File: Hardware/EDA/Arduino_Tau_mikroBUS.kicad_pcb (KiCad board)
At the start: 4 copper layers, 38.1 x 69.8 mm, 30 parts, among them J1 HEADER_F_2.54MM_1R8P_ST_AU_PTH, J2 HEADER_F_2.54MM_1R8P_ST_AU_PTH, J3 HEADER_F_2.54MM_1R11P_ST_AU_P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, J4 HEADER_F_2.54MM_1R11P_ST_AU_P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, J5 Molex_0475710001, M1 FID, M2 FID, M3 FID, P1 HEADER_M_2.54MM_1R4P_ST_AU_PTH, P2 HEADER_M_2.54MM_1R4P_ST_AU_PTH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

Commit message: Updated schematic and gerbers. Added silkscreen artwork and 3D component models.
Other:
- board text added: "Arduino Tau mikroBUS Dev Board"
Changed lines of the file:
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@@
     (area 60.884999 31.674999 99.135001 101.675001)
     (thickness 1.6)
-    (drawings 26)
+    (drawings 27)
     (tracks 249)
     (zones 0)
@@
     (pad 1 thru_hole rect (at -12.7 0 270) (size 1.397 1.397) (drill 0.79375) (layers *.Cu *.Mask F.SilkS)
       (net 5 D5))
+    (model C:/Engineering/KiCAD_Libraries/3D/Headers/VRML/Harwin_M20-7821146.wrl
+      (at (xyz 0 0 0))
+      (scale (xyz 1 1 1))
+      (rotate (xyz 0 0 0))
+    )
   )
   (module Active:SO-8 (layer F.Cu)
@@
     (pad 1 thru_hole rect (at -12.7 0 270) (size 1.397 1.397) (drill 0.79375) (layers *.Cu *.Mask F.SilkS)
       (net 18 D8))
+    (model C:/Engineering/KiCAD_Libraries/3D/Headers/VRML/HEADER_F_2.54MM_1R11P_ST_AU_PTH.wrl
+      (at (xyz 0 0 0))
+      (scale (xyz 1 1 1))
+      (rotate (xyz 0 0 0))
+    )
   )
   (module Passive:0603 (layer F.Cu)
@@
     (pad 4 thru_hole circle (at 3.81 0) (size 1.7272 1.7272) (drill 0.9906) (layers *.Cu *.Mask)
       (net 9 5.0V))
+    (model C:/Engineering/KiCAD_Libraries/3D/Power_Supplies/DC_DC_Converters/VRML/RECOM_RM-0505S.wrl
+      (at (xyz 0 0 0))
+      (scale (xyz 1 1 1))
+      (rotate (xyz 0 0 0))
+    )
+  )
+  (gr_text "Arduino Tau\nmikroBUS\nDev Board" (at 91.186 86.868 90) (layer F.SilkS)
+    (effects (font (size 1.27 1.27) (thickness 0.254)))
   )
   (gr_line (start 67.31 53.34) (end 92.71 53.34) (angle 90) (layer F.SilkS) (width 0.127))
@@
   (segment (start 77.56 45.376) (end 76.708 46.228) (width 0.1524) (layer F.Cu) (net 15))
   (segment (start 90.551 83.185) (end 90.17 82.804) (width 0.4572) (layer F.Cu) (net 16))
-  (segment (start 90.551 99.568) (end 90.551 83.185) (width 0.4572) (layer F.Cu) (net 16) (status 400000))
+  (segment (start 90.551 99.568) (end 90.551 83.185) (width 0.4572) (layer F.Cu) (net 16))
   (segment (start 90.17 82.804) (end 90.17 74.93) (width 0.4572) (layer F.Cu) (net 16))
   (segment (start 68.072 74.93) (end 82.042 74.93) (width 0.4572) (layer F.Cu) (net 16))
@@
   (segment (start 84.582 72.39) (end 87.63 72.39) (width 0.4572) (layer F.Cu) (net 16))
   (segment (start 82.042 74.93) (end 84.582 72.39) (width 0.4572) (layer F.Cu) (net 16))
-  (segment (start 90.17 74.93) (end 91.948 74.93) (width 0.4572) (layer F.Cu) (net 16) (status 800000))
+  (segment (start 90.17 74.93) (end 91.948 74.93) (width 0.4572) (layer F.Cu) (net 16))
   (segment (start 73.66 96.52) (end 74.422 97.282) (width 0.4572) (layer F.Cu) (net 16))
   (segment (start 88.138 99.568) (end 90.551 99.568) (width 0.4572) (layer F.Cu) (net 16))

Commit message: Updated silkscreen artwork and regenerated gerbers.
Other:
- board text added: "61535"
- board text added: "CL-ARDMB-02"
- board text removed: "61xxx"
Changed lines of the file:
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@@
     (links 80)
     (no_connects 0)
-    (area 60.884999 31.674999 99.135001 101.675001)
+    (area 45.184287 23.97 111.025715 109.380001)
     (thickness 1.6)
-    (drawings 27)
+    (drawings 28)
     (tracks 249)
     (zones 0)
@@
     )
   )
+  (gr_text CL-ARDMB-02 (at 71.374 88.138 90) (layer F.SilkS)
+    (effects (font (size 1.016 1.016) (thickness 0.2032)))
+  )
   (gr_text "Arduino Tau\nmikroBUS\nDev Board" (at 91.186 86.868 90) (layer F.SilkS)
     (effects (font (size 1.27 1.27) (thickness 0.254)))
@@
     (arrow2b (pts (xy 57.15 101.6) (xy 56.563579 100.473496)))
   )
-  (gr_text 61xxx (at 65.278 100.076) (layer F.SilkS)
-    (effects (font (size 1.5 1.5) (thickness 0.3)))
-  )
-  (gr_text V1.0 (at 95.758 100.076) (layer F.SilkS)
-    (effects (font (size 1.5 1.5) (thickness 0.3)))
+  (gr_text 61535 (at 64.008 100.33) (layer F.SilkS)
+    (effects (font (size 1.016 1.016) (thickness 0.2032)))
+  )
+  (gr_text V1.0 (at 95.504 84.074 90) (layer F.SilkS)
+    (effects (font (size 1.27 1.27) (thickness 0.254)))
   )
   (gr_text microSD (at 80.264 39.116) (layer F.SilkS)

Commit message: Corrected part# on silkscreen artwork.
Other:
- board text added: "61540"
- board text removed: "61535"
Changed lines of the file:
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@@
     (arrow2b (pts (xy 57.15 101.6) (xy 56.563579 100.473496)))
   )
-  (gr_text 61535 (at 64.008 100.33) (layer F.SilkS)
+  (gr_text 61540 (at 64.008 100.33) (layer F.SilkS)
     (effects (font (size 1.016 1.016) (thickness 0.2032)))
   )

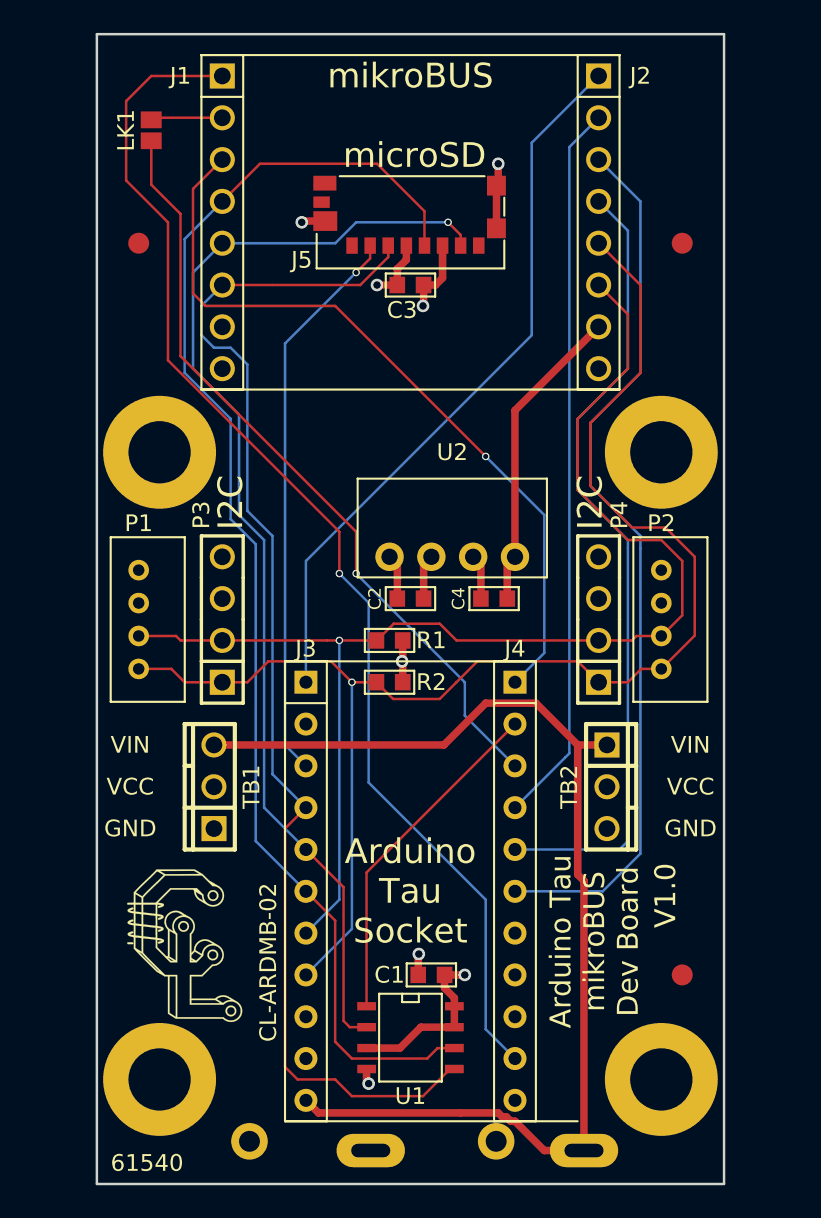
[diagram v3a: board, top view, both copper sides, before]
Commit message: Changed PCB outline/size to accomodate mounting holes, but still fit in enclosure. Regenerated Gerbers and PCB render images.
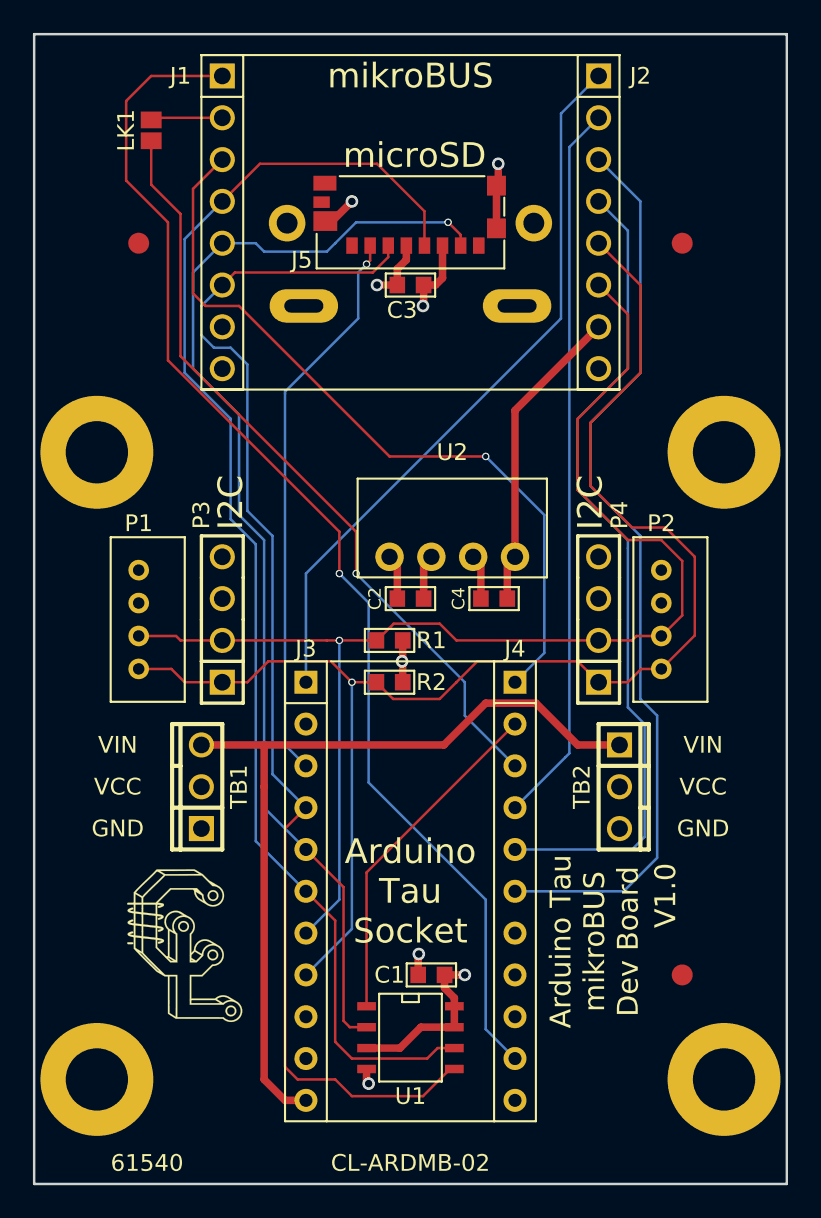
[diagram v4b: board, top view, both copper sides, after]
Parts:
- moved B1 51.5 mm to (80.0, 48.3), turned to 270 degrees
- moved MH2 3.81 mm to (99.1, 57.1)
- moved MH4 3.81 mm to (99.1, 95.2)
- moved MH1 3.81 mm to (61.0, 57.1)
- moved MH3 3.81 mm to (61.0, 95.2)
- moved B2 2.29 mm to (80.0, 71.1), turned to 90 degrees
- moved TB1 0.76 mm to (67.3, 77.5)
- moved TB2 0.76 mm to (92.7, 77.5)
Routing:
- net VIN: track 68.9 -> 80.9 mm
- net RXD: track 54.3 -> 55.9 mm
- net TXD: track 49.2 -> 50.5 mm
- net GND: track 17.7 -> 18.4 mm
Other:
- board size 38.1 x 69.8 mm -> 45.7 x 69.8 mm

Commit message: Finished updates.
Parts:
- U1: value FL127 -> FL116K
- moved M1 2.54 mm to (99.1, 88.9)
- moved M2 2.54 mm to (99.1, 44.5)
- moved M3 2.54 mm to (61.0, 44.5)
- moved LK1 1.30 mm to (63.0, 37.3)
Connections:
- net mikroBUS_RST renamed /mikroBUS_RST
- J3 pad 2: (no net) -> D9
- J4 pad 7: (no net) -> AREF
- J4 pad 8: (no net) -> A4
- J4 pad 9: (no net) -> A3
- J5 pad 1: (no net) -> Net-(J5-Pad1)
- J5 pad 12: (no net) -> Net-(J5-Pad12)
- J5 pad 13: (no net) -> Net-(J5-Pad13)
- J5 pad 8: (no net) -> Net-(J5-Pad8)
- M1 pad ~: (no net) -> Net-(M1-Pad~)
- M2 pad ~: (no net) -> Net-(M2-Pad~)
- M3 pad ~: (no net) -> Net-(M3-Pad~)
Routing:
- net VIN: track 80.9 -> 86.2 mm
- net A0: track 74.4 -> 76.2 mm
- net /mikroBUS_RST: track 4.37 -> 5.64 mm
- net D3: track 47.1 -> 47.9 mm
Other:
- board text added: "3.3V"
- board text added: "5.0V"
- board text added: "AN"
- board text added: "CS"
- board text added: "Corrections made: Add silkscreen pin names to mikroBUS connector Corrected pin numbering of 2xAA battery holder footprint to match schematic decal Corrected pin numbering of 1x9V battery holder footprint to match schematic decal Re-layed out 2xAA battery traces Re-layed out 1x9V battery traces Added silkscreen pin names to Grove connector Add silkscreen orientation to Arduino socket"
- board text added: "Corrections needed: Check FL127 footprint against Winbond footprint"
- board text added: "INT"
- board text added: "MISO"
- board text added: "MOSI"
- board text added: "PWM"
- board text added: "RST"
- board text added: "RXD"
- board text added: "SCK"
- board text added: "SCL"
- board text added: "SDA"
- board text added: "TXD"
- board text added: "V1.1"
- board text removed: "V1.0"

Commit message: Final changes prior to gerber verification.
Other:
- board text added: "Corrections made: Add silkscreen pin names to mikroBUS connector Corrected pin numbering of 2xAA battery holder footprint to match schematic decal Corrected pin numbering of 1x9V battery holder footprint to match schematic decal Re-layed out 2xAA battery traces Re-layed out 1x9V battery traces Added silkscreen pin names to Grove connector Add silkscreen orientation to Arduino socket Verified thro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"
- board text added: "Corrections needed:"
- board text removed: "Corrections made: Add silkscreen pin names to mikroBUS connector Corrected pin numbering of 2xAA battery holder footprint to match schematic decal Corrected pin numbering of 1x9V battery holder footprint to match schematic decal Re-layed out 2xAA battery traces Re-layed out 1x9V battery traces Added silkscreen pin names to Grove connector Add silkscreen orientation to Arduino socket"
- board text removed: "Corrections needed: Check FL127 footprint against Winbond footprint"
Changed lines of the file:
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@@
-(kicad_pcb (version 4) (host pcbnew 4.0.6)
+(kicad_pcb (version 4) (host pcbnew 4.0.4-stable)
   (general
     (links 80)
     (no_connects 0)
-    (area 57.074999 31.674999 102.945001 101.675001)
+    (area 41.374287 23.97 225.341426 113.190001)
     (thickness 1.6)
     (drawings 57)
@@
     (add_net VIN)
   )
+  (module Battery:Keystone_2462_2AA locked (layer B.Cu)
+    (at 80.01 71.12 90)
+    (fp_text reference B2 (at 31.75 0 360) (layer B.SilkS)
+      (effects (font (size 1.016 1.016) (thickness 0.1524)) (justify mirror))
+    )
+    (fp_text value 2xAA (at -31.75 0 180) (layer B.Fab)
+      (effects (font (size 1.016 1.016) (thickness 0.1524)) (justify mirror))
+    )
+    (fp_line (start 27.432 -4.826) (end 28.448 -4.826) (layer B.SilkS) (width 0.127))
+    (fp_circle (center 27.94 -4.826) (end 28.956 -4.826) (layer B.SilkS) (width 0.127))
+    (fp_line (start 27.94 -4.318) (end 27.94 -5.334) (layer B.SilkS) (width 0.127))
+    (fp_line (start 27.94 5.334) (end 27.94 4.318) (layer B.SilkS) (width 0.127))
+    (fp_circle (center 27.94 4.826) (end 28.956 4.826) (layer B.SilkS) (width 0.127))
+    (fp_line (start -30.48 16.51) (end -30.48 -16.51) (layer B.SilkS) (width 0.127))
+    (fp_line (start -30.48 -16.51) (end 30.48 -16.51) (layer B.SilkS) (width 0.127))
+    (fp_line (start 30.48 -16.51) (end 30.48 16.51) (layer B.SilkS) (width 0.127))
+    (fp_line (start 30.48 16.51) (end -30.48 16.51) (layer B.SilkS) (width 0.127))
+    (pad 2 thru_hole circle (at 27.8892 7.493 90) (size 2.2225 2.2225) (drill 1.27) (layers *.Cu *.Mask)
+      (net 1 GND))
+    (pad 1 thru_hole circle (at 27.8892 -7.493 90) (size 2.2225 2.2225) (drill 1.27) (layers *.Cu *.Mask)
+      (net 16 3V3))
+    (model C:/Engineering/KiCAD_Libraries/3D/Battery_Holders/VRML/KEYSTONE_2462.wrl_
+      (at (xyz 0.03 0 0))
+      (scale (xyz 1 1 1))
+      (rotate (xyz 0 0 0))
+    )
+  )
   (module Battery:BC9VPC locked (layer B.Cu)
     (at 80.01 48.26 270)
@@
     (model C:/Engineering/KiCAD_Libraries/3D/Battery_Holders/VRML/Memory_Protection_Devices_BC9VPC.wrl_
       (at (xyz 0 0 0))
-      (scale (xyz 1 1 1))
-      (rotate (xyz 0 0 0))
-    )
-  )
-  (module Battery:Keystone_2462_2AA locked (layer B.Cu)
-    (at 80.01 71.12 90)
-    (fp_text reference B2 (at 31.75 0 360) (layer B.SilkS)
-      (effects (font (size 1.016 1.016) (thickness 0.1524)) (justify mirror))
-    )
-    (fp_text value 2xAA (at -31.75 0 180) (layer B.Fab)
-      (effects (font (size 1.016 1.016) (thickness 0.1524)) (justify mirror))
-    )
-    (fp_line (start 24.892 -7.62) (end 25.908 -7.62) (layer B.SilkS) (width 0.127))
-    (fp_circle (center 25.4 -7.62) (end 26.416 -7.62) (layer B.SilkS) (width 0.127))
-    (fp_line (start 25.4 -7.112) (end 25.4 -8.128) (layer B.SilkS) (width 0.127))
-    (fp_line (start 25.4 8.128) (end 25.4 7.112) (layer B.SilkS) (width 0.127))
-    (fp_circle (center 25.4 7.62) (end 26.416 7.62) (layer B.SilkS) (width 0.127))
-    (fp_line (start -30.48 16.51) (end -30.48 -16.51) (layer B.SilkS) (width 0.127))
-    (fp_line (start -30.48 -16.51) (end 30.48 -16.51) (layer B.SilkS) (width 0.127))
-    (fp_line (start 30.48 -16.51) (end 30.48 16.51) (layer B.SilkS) (width 0.127))
-    (fp_line (start 30.48 16.51) (end -30.48 16.51) (layer B.SilkS) (width 0.127))
-    (pad 2 thru_hole circle (at 27.8892 7.493 90) (size 2.2225 2.2225) (drill 1.27) (layers *.Cu *.Mask)
-      (net 1 GND))
-    (pad 1 thru_hole circle (at 27.8892 -7.493 90) (size 2.2225 2.2225) (drill 1.27) (layers *.Cu *.Mask)
-      (net 16 3V3))
-    (model C:/Engineering/KiCAD_Libraries/3D/Battery_Holders/VRML/KEYSTONE_2462.wrl
-      (at (xyz 0.03 0 0))
       (scale (xyz 1 1 1))
       (rotate (xyz 0 0 0))
@@
     (effects (font (size 1.016 1.016) (thickness 0.2032)))
   )
-  (gr_text "Corrections needed:\nCheck FL127 footprint against Winbond footprint\n" (at 128.27 39.37) (layer Cmts.User)
+  (gr_text "Corrections needed:\n\n" (at 128.27 39.37) (layer Cmts.User)
     (effects (font (size 1.5 1.5) (thickness 0.3)) (justify left))
   )
-  (gr_text "Corrections made:\nAdd silkscreen pin names to mikroBUS connector\nCorrected pin numbering of 2xAA battery holder footprint to match schematic decal\nCorrected pin numbering of 1x9V battery holder footprint to match schematic decal\nRe-layed out 2xAA battery traces\nRe-layed out 1x9V battery traces\nAdded silkscreen pin names to Grove connector\nAdd silkscreen orientation to Arduino socket\n" (at 128.27 69.85) (layer Cmts.User)
+  (gr_text "Corrections made:\nAdd silkscreen pin names to mikroBUS connector\nCorrected pin numbering of 2xAA battery holder footprint to match schematic decal\nCorrected pin numbering of 1x9V battery holder footprint to match schematic decal\nRe-layed out 2xAA battery traces\nRe-layed out 1x9V battery traces\nAdded silkscreen pin names to Grove connector\nAdd silkscreen orientation to Arduino socket\nVerified through testing Flash chip is functional\n" (at 128.27 69.85) (layer Cmts.User)
     (effects (font (size 1.5 1.5) (thickness 0.3)) (justify left))
   )

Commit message: Moved two traces near MH2. Verified gerbers.
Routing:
- net SCL: track 87.1 -> 83.4 mm
- net SDA: track 79.1 -> 75.4 mm
- net RXD: track 55.9 -> 53.4 mm
- net TXD: track 50.5 -> 48.0 mm
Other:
- board text removed: "Corrections made: Add silkscreen pin names to mikroBUS connector Corrected pin numbering of 2xAA battery holder footprint to match schematic decal Corrected pin numbering of 1x9V battery holder footprint to match schematic decal Re-layed out 2xAA battery traces Re-layed out 1x9V battery traces Added silkscreen pin names to Grove connector Add silkscreen orientation to Arduino socket Verified thro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"
- board text removed: "Corrections needed:"
